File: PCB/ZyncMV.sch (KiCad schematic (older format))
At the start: 0 parts

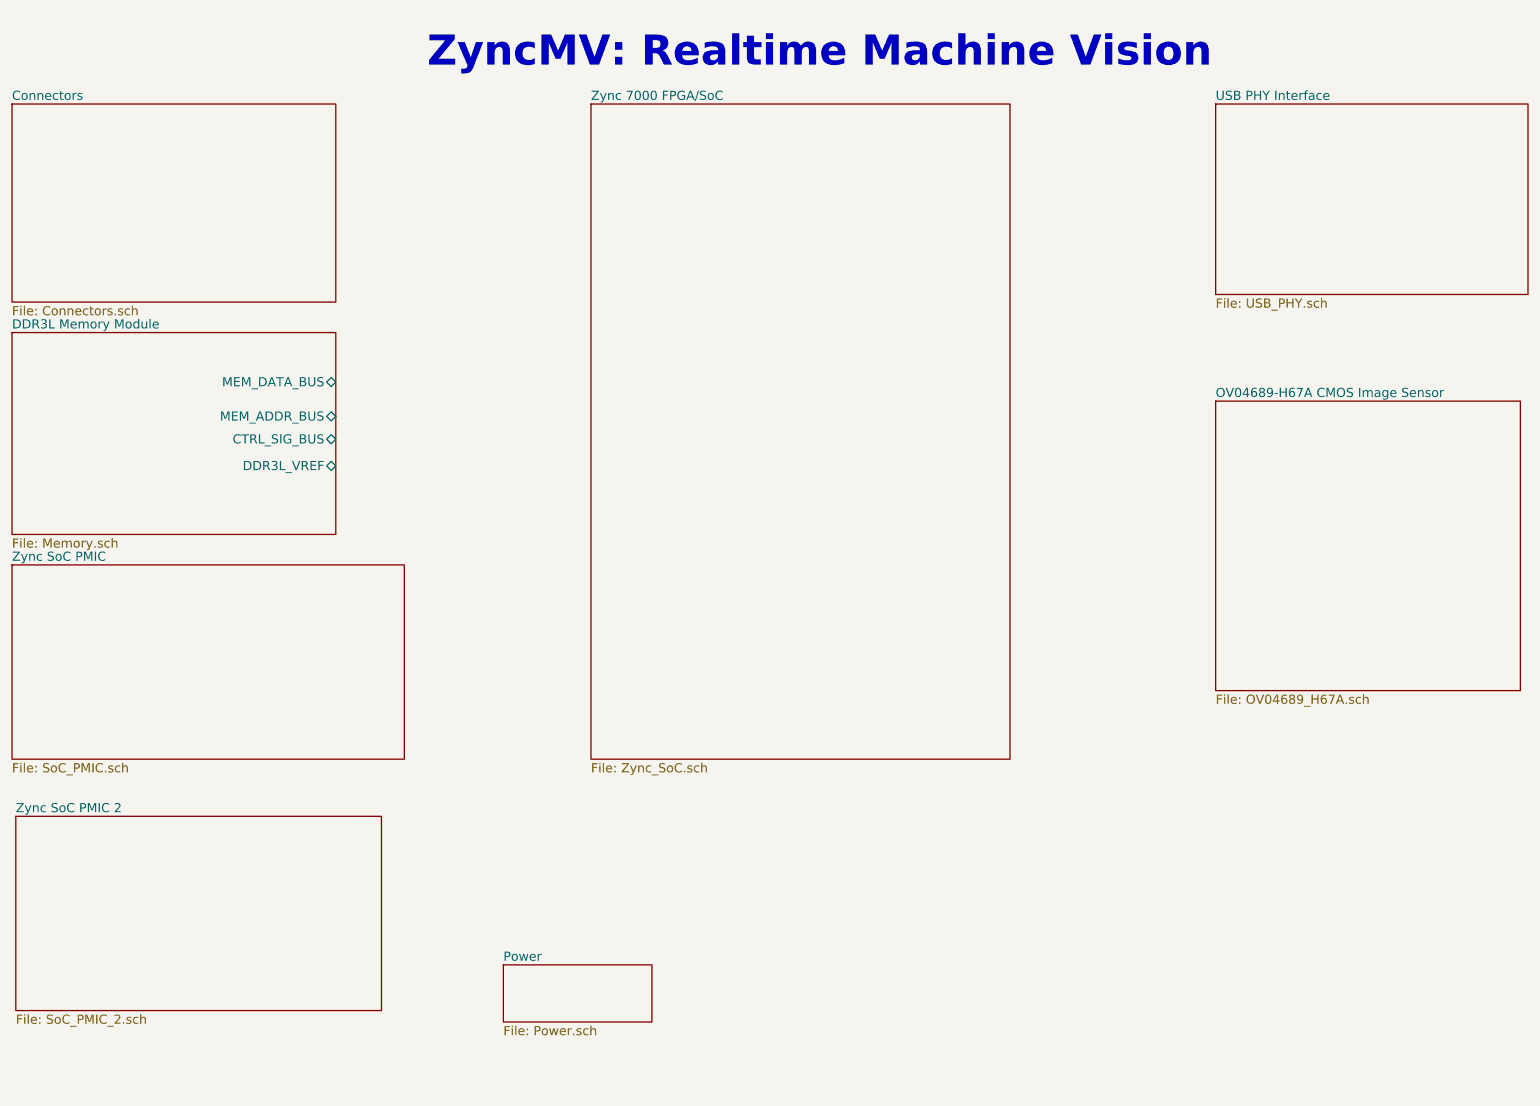
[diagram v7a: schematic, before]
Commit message: Memory and Camera
Memory and Camera schematics tentatively complete. They are subject to
change as all hardware projects are.
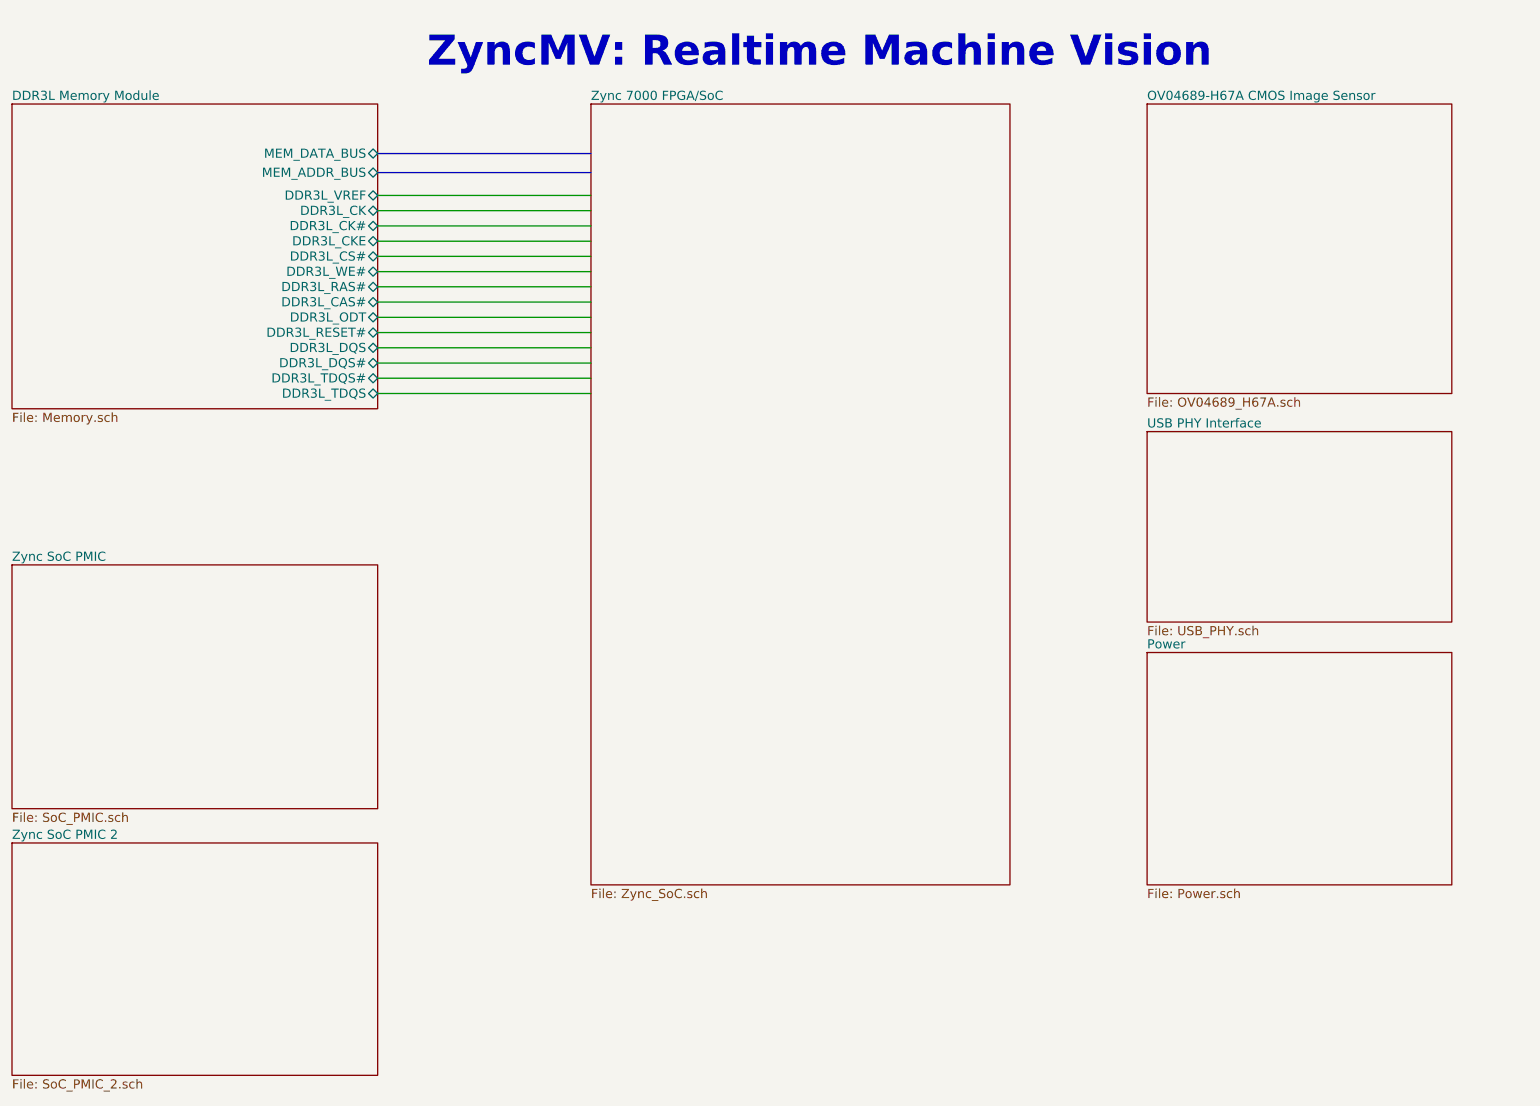
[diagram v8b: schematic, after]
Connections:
- wire segments 0 -> 14
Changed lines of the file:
@@
 $Descr A4 11693 8268
 encoding utf-8
-Sheet 1 9
+Sheet 1 8
 Title ""
 Date "2016-12-23"
@@
 $EndDescr
 $Sheet
-S 4700 1275 2750 4300
+S 4700 1275 2750 5125
 U 585AE0B8
 F0 "Zync 7000 FPGA/SoC" 60
@@
 $EndSheet
 $Sheet
-S 4125 6925 975  375
+S 8350 4875 2000 1525
 U 585AE0DE
 F0 "Power" 60
@@
 $EndSheet
 $Sheet
-S 8800 3225 2000 1900
+S 8350 1275 2000 1900
 U 585AE0EB
 F0 "OV04689-H67A CMOS Image Sensor" 60
@@
 $EndSheet
 $Sheet
-S 900  2775 2125 1325
+S 900  1275 2400 2000
 U 585AE128
 F0 "DDR3L Memory Module" 60
 F1 "Memory.sch" 60
-F2 "MEM_DATA_BUS" B R 3025 3100 60
-F3 "MEM_ADDR_BUS" B R 3025 3325 60
-F4 "CTRL_SIG_BUS" B R 3025 3475 60
-F5 "DDR3L_VREF" B R 3025 3650 60
+F2 "MEM_DATA_BUS" B R 3300 1600 60
+F3 "MEM_ADDR_BUS" B R 3300 1725 60
+F4 "DDR3L_VREF" B R 3300 1875 60
+F5 "DDR3L_CK" B R 3300 1975 60
+F6 "DDR3L_CK#" B R 3300 2075 60
+F7 "DDR3L_CKE" B R 3300 2175 60
+F8 "DDR3L_CS#" B R 3300 2275 60
+F9 "DDR3L_WE#" B R 3300 2375 60
+F10 "DDR3L_RAS#" B R 3300 2475 60
+F11 "DDR3L_CAS#" B R 3300 2575 60
+F12 "DDR3L_ODT" B R 3300 2675 60
+F13 "DDR3L_RESET#" B R 3300 2775 60
+F14 "DDR3L_DQS" B R 3300 2875 60
+F15 "DDR3L_DQS#" B R 3300 2975 60
+F16 "DDR3L_TDQS#" B R 3300 3075 60
+F17 "DDR3L_TDQS" B R 3300 3175 60
 $EndSheet
 $Sheet
-S 900  1275 2125 1300
-U 585AE13E
-F0 "Connectors" 60
-F1 "Connectors.sch" 60
-$EndSheet
-$Sheet
-S 8800 1275 2050 1250
+S 8350 3425 2000 1250
 U 585AE27C
 F0 "USB PHY Interface" 60
@@
 ZyncMV: Realtime Machine Vision
 $Sheet
-S 900  4300 2575 1275
+S 900  4300 2400 1600
 U 5878744A
 F0 "Zync SoC PMIC" 60
@@
 $EndSheet
 $Sheet
-S 925  5950 2400 1275
+S 900  6125 2400 1525
 U 5878DB5C
 F0 "Zync SoC PMIC 2" 60
 F1 "SoC_PMIC_2.sch" 60
 $EndSheet
+Wire Bus Line
+	3300 1600 4700 1600
+Wire Bus Line
+	3300 1725 4700 1725
+Wire Wire Line
+	3300 1875 4700 1875
+Wire Wire Line
+	3300 1975 4700 1975
+Wire Wire Line
+	3300 2075 4700 2075
+Wire Wire Line
+	3300 2175 4700 2175
+Wire Wire Line
+	3300 2275 4700 2275
+Wire Wire Line
+	3300 2375 4700 2375
+Wire Wire Line
+	3300 2475 4700 2475
+Wire Wire Line
+	3300 2575 4700 2575
+Wire Wire Line
+	3300 2675 4700 2675
+Wire Wire Line
+	3300 2775 4700 2775
+Wire Wire Line
+	3300 2875 4700 2875
+Wire Wire Line
+	3300 2975 4700 2975
+Wire Wire Line
+	3300 3075 4700 3075
+Wire Wire Line
+	3300 3175 4700 3175
 $EndSCHEMATC
